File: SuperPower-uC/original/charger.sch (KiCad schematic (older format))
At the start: 24 parts, among them J2 NTC connector, J3 DNP/JST_XH_S2B_thru, Q2 DMN3018SSD, Q3 2N7002A, Q4 DMP3028LSD, U2 LTC4162EUFD-LAD

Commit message: Assigned footprint to resistors 0603 and connectors
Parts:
- C2, C3: footprint Capacitor_SMD:C_0805_2012Metric -> Capacitors_SMD:C_0805
- C4, C5: footprint Capacitor_SMD:C_0603_1608Metric -> Capacitors_SMD:C_0603
- C6, C7: footprint Capacitor_SMD:C_1206_3216Metric -> Capacitors_SMD:C_1206
- R10, R12, R13, R14, R6, R8, R9: footprint (none) -> Resistors_SMD:R_0603
- R11, R7: footprint (none) -> Resistors_SMD:R_0805
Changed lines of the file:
@@
 F 0 "R7" V 4495 2800 50  0000 C CNN
 F 1 "68m" V 4586 2800 50  0000 C CNN
-F 2 "" V 4740 2790 50  0001 C CNN
+F 2 "Resistors_SMD:R_0805" V 4740 2790 50  0001 C CNN
 F 3 "~" H 4700 2800 50  0001 C CNN
 	1    4700 2800
@@
 F 0 "R11" H 7518 4196 50  0000 L CNN
 F 1 "68m" H 7518 4105 50  0000 L CNN
-F 2 "" V 7490 4140 50  0001 C CNN
+F 2 "Resistors_SMD:R_0805" V 7490 4140 50  0001 C CNN
 F 3 "~" H 7450 4150 50  0001 C CNN
 	1    7450 4150
@@
 F 0 "R9" V 6195 4700 50  0000 C CNN
 F 1 "10k" V 6286 4700 50  0000 C CNN
-F 2 "" V 6440 4690 50  0001 C CNN
+F 2 "Resistors_SMD:R_0603" V 6440 4690 50  0001 C CNN
 F 3 "~" H 6400 4700 50  0001 C CNN
 	1    6400 4700
@@
 F 0 "R13" H 7118 2096 50  0000 L CNN
 F 1 "390k" H 7118 2005 50  0000 L CNN
-F 2 "" V 7090 2040 50  0001 C CNN
+F 2 "Resistors_SMD:R_0603" V 7090 2040 50  0001 C CNN
 F 3 "~" H 7050 2050 50  0001 C CNN
 	1    7050 2050
@@
 F 0 "R10" H 6668 1696 50  0000 L CNN
 F 1 "1M" H 6668 1605 50  0000 L CNN
-F 2 "" V 6640 1640 50  0001 C CNN
+F 2 "Resistors_SMD:R_0603" V 6640 1640 50  0001 C CNN
 F 3 "~" H 6600 1650 50  0001 C CNN
 	1    6600 1650
@@
 F 0 "R12" V 6845 850 50  0000 C CNN
 F 1 "DNP/0" V 6936 850 50  0000 C CNN
-F 2 "" V 7090 840 50  0001 C CNN
+F 2 "Resistors_SMD:R_0603" V 7090 840 50  0001 C CNN
 F 3 "~" H 7050 850 50  0001 C CNN
 	1    7050 850
@@
 F 0 "R6" V 2345 3750 50  0000 C CNN
 F 1 "2.2k" V 2436 3750 50  0000 C CNN
-F 2 "" V 2590 3740 50  0001 C CNN
+F 2 "Resistors_SMD:R_0603" V 2590 3740 50  0001 C CNN
 F 3 "~" H 2550 3750 50  0001 C CNN
 	1    2550 3750
@@
 F 0 "R8" H 5232 5304 50  0000 R CNN
 F 1 "63.4k" H 5232 5395 50  0000 R CNN
-F 2 "" V 5340 5340 50  0001 C CNN
+F 2 "Resistors_SMD:R_0603" V 5340 5340 50  0001 C CNN
 F 3 "~" H 5300 5350 50  0001 C CNN
 	1    5300 5350
@@
 F 0 "R14" V 6195 5100 50  0000 C CNN
 F 1 "10k" V 6286 5100 50  0000 C CNN
-F 2 "" V 6440 5090 50  0001 C CNN
+F 2 "Resistors_SMD:R_0603" V 6440 5090 50  0001 C CNN
 F 3 "~" H 6400 5100 50  0001 C CNN
 	1    6400 5100
@@
 F 0 "C7" H 8415 3532 50  0000 L CNN
 F 1 "CL31B106KAHNNNE" H 8325 3250 50  0001 L CNN
-F 2 "Capacitor_SMD:C_1206_3216Metric" H 8338 3200 50  0001 C CNN
+F 2 "Capacitors_SMD:C_1206" H 8338 3200 50  0001 C CNN
 F 3 "https://eu.mouser.com/datasheet/2/585/MLCC-1837944.pdf" H 8300 3350 50  0001 C CNN
 F 4 "Samsung" H 8300 3350 50  0001 C CNN "Mfr_name"
@@
 F 0 "C6" H 7565 4782 50  0000 L CNN
 F 1 "CL31B106KAHNNNE" H 7475 4500 50  0001 L CNN
-F 2 "Capacitor_SMD:C_1206_3216Metric" H 7488 4450 50  0001 C CNN
+F 2 "Capacitors_SMD:C_1206" H 7488 4450 50  0001 C CNN
 F 3 "https://eu.mouser.com/datasheet/2/585/MLCC-1837944.pdf" H 7450 4600 50  0001 C CNN
 F 4 "Samsung" H 7450 4600 50  0001 C CNN "Mfr_name"
@@
 F 0 "C2" H 3465 3232 50  0000 L CNN
 F 1 "CC0603JRX7R9BB104" H 3375 2950 50  0001 L CNN
-F 2 "Capacitor_SMD:C_0805_2012Metric" H 3388 2900 50  0001 C CNN
+F 2 "Capacitors_SMD:C_0805" H 3388 2900 50  0001 C CNN
 F 3 "https://www.yageo.com/upload/media/product/productsearch/datasheet/mlcc/UPY-GPHC_X7R_6.3V-to-50V_20.pdf" H 3350 3050 50  0001 C CNN
 F 4 "Yageo" H 3350 3050 50  0001 C CNN "Mfr_name"
@@
 F 0 "C4" H 4865 5082 50  0000 L CNN
 F 1 "CL10B105KO8NNNC" H 4775 4800 50  0001 L CNN
-F 2 "Capacitor_SMD:C_0603_1608Metric" H 4788 4750 50  0001 C CNN
+F 2 "Capacitors_SMD:C_0603" H 4788 4750 50  0001 C CNN
 F 3 "" H 4750 4900 50  0001 C CNN
 F 4 "Samsung" H 4750 4900 50  0001 C CNN "Mfr_name"
@@
 F 0 "C3" H 4365 5082 50  0000 L CNN
 F 1 "TMK212AB7475KG-T" H 4275 4800 50  0001 L CNN
-F 2 "Capacitor_SMD:C_0805_2012Metric" H 4288 4750 50  0001 C CNN
+F 2 "Capacitors_SMD:C_0805" H 4288 4750 50  0001 C CNN
 F 3 "https://eu.mouser.com/datasheet/2/396/mlcc02_e-1307760.pdf" H 4250 4900 50  0001 C CNN
 F 4 "Taiyo Yuden" H 4250 4900 50  0001 C CNN "Mfr_name"
@@
 F 0 "C5" H 6515 3832 50  0000 L CNN
 F 1 "CL10B223KB8NNNC" H 6425 3550 50  0001 L CNN
-F 2 "Capacitor_SMD:C_0603_1608Metric" H 6438 3500 50  0001 C CNN
+F 2 "Capacitors_SMD:C_0603" H 6438 3500 50  0001 C CNN
 F 3 "" H 6400 3650 50  0001 C CNN
 F 4 "CL10B223KB8NNNC" H 6400 3650 50  0001 C CNN "Mfr_no"

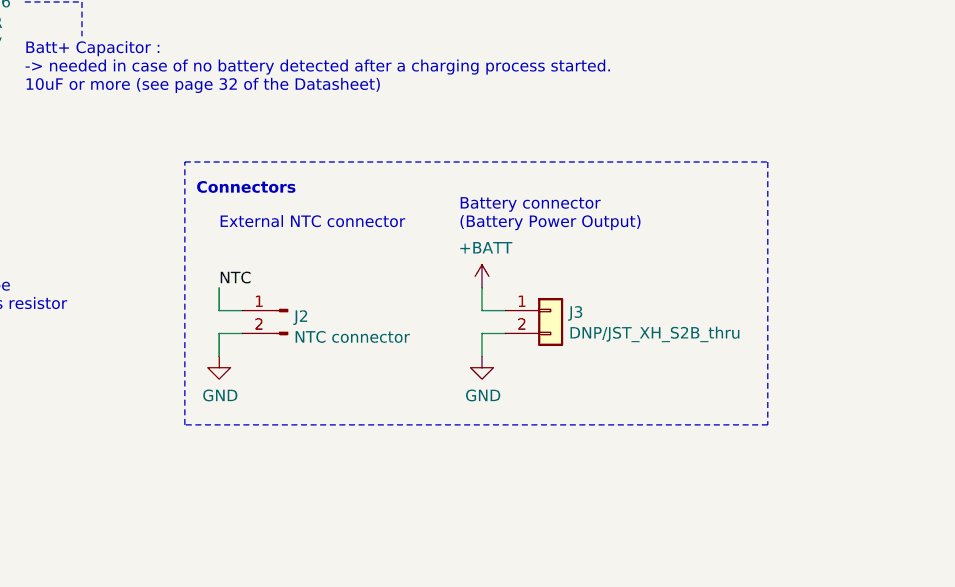
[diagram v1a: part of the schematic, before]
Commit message: Update NTC Connector & USB-C Library path
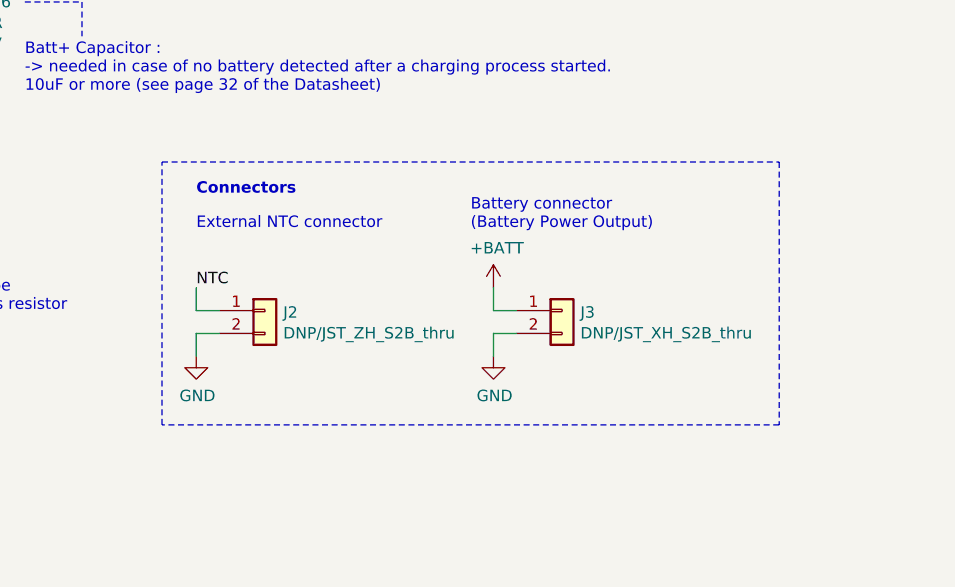
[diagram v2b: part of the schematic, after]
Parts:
- removed J2: NTC connector, symbol Connector:Conn_01x02_Male
- added J2: DNP/JST_ZH_S2B_thru, Connector_JST_user:JST_ZH_S2B-ZR_1x02_P1.50mm_Horizontal, symbol jst_zh_s2b_thru:JST_ZH_S2B_thru
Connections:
- net GND: now also J2.2 (Pin_2)
- net NTC: now also J2.1 (Pin_1)
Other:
- moved on the sheet: J3

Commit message: Updated footprints and fixed issues
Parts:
- J2: footprint Connector_JST_user:JST_ZH_S2B-ZR_1x02_P1.50mm_Horizontal -> JST_ZH_S2B_THRU:JST_ZH_S2B-ZR_1x02_P1.50mm_Horizontal
- J3: footprint Connector_JST:JST_XH_S2B-XH-A_1x02_P2.50mm_Horizontal -> Connectors_JST:JST_XH_S02B-XH-A_02x2.50mm_Angled
- LED1: footprint (none) -> LEDs:LED_0603
- Q3: footprint Package_TO_SOT_SMD:SOT-23 -> TO_SOT_Packages_SMD:SOT-23
- U2: footprint Package_DFN_QFN:QFN-28-1EP_4x5mm_P0.5mm_EP2.65x3.65mm_ThermalVias -> Housings_DFN_QFN:QFN-28-1EP_4x5mm_Pitch0.5mm
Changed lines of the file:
@@
 F 0 "U2" H 5200 5050 50  0000 C CNN
 F 1 "LTC4162EUFD-LAD" H 5950 5050 50  0000 C CNN
-F 2 "Package_DFN_QFN:QFN-28-1EP_4x5mm_P0.5mm_EP2.65x3.65mm_ThermalVias" H 5250 5050 50  0001 C CNN
+F 2 "Housings_DFN_QFN:QFN-28-1EP_4x5mm_Pitch0.5mm" H 5250 5050 50  0001 C CNN
 F 3 "https://www.analog.com/media/en/technical-documentation/data-sheets/LTC4162-L.pdf" H 5200 5050 50  0001 C CNN
 F 4 "https://octopart.com/ltc4162eufd-lad%23pbf-analog+devices-92333982?r=sp" H 5600 4000 50  0001 C CNN "Octopart_link"
@@
 F 0 "LED1" H 2143 3495 50  0000 C CNN
 F 1 "150060YS75000_0603" H 2143 3586 50  0001 C CNN
-F 2 "" H 2150 3750 50  0001 C CNN
+F 2 "LEDs:LED_0603" H 2150 3750 50  0001 C CNN
 F 3 "~" H 2150 3750 50  0001 C CNN
 F 4 "Wurth Elektronik " H 2150 3750 50  0001 C CNN "Mfr_name"
@@
 F 0 "J3" H 10230 5942 50  0000 L CNN
 F 1 "DNP/JST_XH_S2B_thru" H 10230 5851 50  0000 L CNN
-F 2 "Connector_JST:JST_XH_S2B-XH-A_1x02_P2.50mm_Horizontal" H 10150 5950 50  0001 C CNN
+F 2 "Connectors_JST:JST_XH_S02B-XH-A_02x2.50mm_Angled" H 10150 5950 50  0001 C CNN
 F 3 "http://www.jst-mfg.com/product/pdf/eng/eXH.pdf" H 10150 5950 50  0001 C CNN
 F 4 "JST" H 10150 5950 50  0001 C CNN "Mfr_name"
@@
 F 0 "Q3" H 7155 2587 50  0000 L CNN
 F 1 "2N7002A" H 7155 2496 50  0000 L CNN
-F 2 "Package_TO_SOT_SMD:SOT-23" H 7150 2375 50  0001 L CNN
+F 2 "TO_SOT_Packages_SMD:SOT-23" H 7150 2375 50  0001 L CNN
 F 3 "https://www.diodes.com/assets/Datasheets/ds31360.pdf" H 6950 2450 50  0001 C CNN
 F 4 "Diodes Incorporated" H 6950 2450 50  0001 C CNN "Mfr_name"
@@
 F 0 "J2" H 8930 5942 50  0000 L CNN
 F 1 "DNP/JST_ZH_S2B_thru" H 8930 5851 50  0000 L CNN
-F 2 "Connector_JST_user:JST_ZH_S2B-ZR_1x02_P1.50mm_Horizontal" H 8850 5950 50  0001 C CNN
+F 2 "JST_ZH_S2B_THRU:JST_ZH_S2B-ZR_1x02_P1.50mm_Horizontal" H 8850 5950 50  0001 C CNN
 F 3 "http://www.jst-mfg.com/product/pdf/eng/eZH.pdf" H 8850 5950 50  0001 C CNN
 F 4 "JST" H 8850 5950 50  0001 C CNN "Mfr_name"

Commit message: reassigned most footprints
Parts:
- C2, C3: footprint Capacitors_SMD:C_0805 -> Capacitor_SMD:C_0805_2012Metric
- C4, C5: footprint Capacitors_SMD:C_0603 -> Capacitor_SMD:C_0603_1608Metric
- C6, C7: footprint Capacitors_SMD:C_1206 -> Capacitor_SMD:C_1206_3216Metric
- J3: footprint Connectors_JST:JST_XH_S02B-XH-A_02x2.50mm_Angled -> Connector_JST:JST_XH_S2B-XH-A-1_1x02_P2.50mm_Horizontal
- LED1: footprint LEDs:LED_0603 -> LED_SMD:LED_0603_1608Metric
- Q3: footprint TO_SOT_Packages_SMD:SOT-23 -> Package_TO_SOT_SMD:SOT-23
- R10, R12, R13, R14, R6, R8, R9: footprint Resistors_SMD:R_0603 -> Resistor_SMD:R_0603_1608Metric
- R11, R7: footprint Resistors_SMD:R_0805 -> Resistor_SMD:R_0805_2012Metric
- U2: footprint Housings_DFN_QFN:QFN-28-1EP_4x5mm_Pitch0.5mm -> Package_DFN_QFN:QFN-28-1EP_4x5mm_P0.5mm_EP2.65x3.65mm_ThermalVias
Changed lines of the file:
@@
 F 0 "R7" V 4495 2800 50  0000 C CNN
 F 1 "68m" V 4586 2800 50  0000 C CNN
-F 2 "Resistors_SMD:R_0805" V 4740 2790 50  0001 C CNN
+F 2 "Resistor_SMD:R_0805_2012Metric" V 4740 2790 50  0001 C CNN
 F 3 "~" H 4700 2800 50  0001 C CNN
 	1    4700 2800
@@
 F 0 "R11" H 7518 4196 50  0000 L CNN
 F 1 "68m" H 7518 4105 50  0000 L CNN
-F 2 "Resistors_SMD:R_0805" V 7490 4140 50  0001 C CNN
+F 2 "Resistor_SMD:R_0805_2012Metric" V 7490 4140 50  0001 C CNN
 F 3 "~" H 7450 4150 50  0001 C CNN
 	1    7450 4150
@@
 F 0 "R9" V 6195 4700 50  0000 C CNN
 F 1 "10k" V 6286 4700 50  0000 C CNN
-F 2 "Resistors_SMD:R_0603" V 6440 4690 50  0001 C CNN
+F 2 "Resistor_SMD:R_0603_1608Metric" V 6440 4690 50  0001 C CNN
 F 3 "~" H 6400 4700 50  0001 C CNN
 	1    6400 4700
@@
 F 0 "R13" H 7118 2096 50  0000 L CNN
 F 1 "390k" H 7118 2005 50  0000 L CNN
-F 2 "Resistors_SMD:R_0603" V 7090 2040 50  0001 C CNN
+F 2 "Resistor_SMD:R_0603_1608Metric" V 7090 2040 50  0001 C CNN
 F 3 "~" H 7050 2050 50  0001 C CNN
 	1    7050 2050
@@
 F 0 "R10" H 6668 1696 50  0000 L CNN
 F 1 "1M" H 6668 1605 50  0000 L CNN
-F 2 "Resistors_SMD:R_0603" V 6640 1640 50  0001 C CNN
+F 2 "Resistor_SMD:R_0603_1608Metric" V 6640 1640 50  0001 C CNN
 F 3 "~" H 6600 1650 50  0001 C CNN
 	1    6600 1650
@@
 F 0 "R12" V 6845 850 50  0000 C CNN
 F 1 "DNP/0" V 6936 850 50  0000 C CNN
-F 2 "Resistors_SMD:R_0603" V 7090 840 50  0001 C CNN
+F 2 "Resistor_SMD:R_0603_1608Metric" V 7090 840 50  0001 C CNN
 F 3 "~" H 7050 850 50  0001 C CNN
 	1    7050 850
@@
 F 0 "R6" V 2345 3750 50  0000 C CNN
 F 1 "2.2k" V 2436 3750 50  0000 C CNN
-F 2 "Resistors_SMD:R_0603" V 2590 3740 50  0001 C CNN
+F 2 "Resistor_SMD:R_0603_1608Metric" V 2590 3740 50  0001 C CNN
 F 3 "~" H 2550 3750 50  0001 C CNN
 	1    2550 3750
@@
 F 0 "R8" H 5232 5304 50  0000 R CNN
 F 1 "63.4k" H 5232 5395 50  0000 R CNN
-F 2 "Resistors_SMD:R_0603" V 5340 5340 50  0001 C CNN
+F 2 "Resistor_SMD:R_0603_1608Metric" V 5340 5340 50  0001 C CNN
 F 3 "~" H 5300 5350 50  0001 C CNN
 	1    5300 5350
@@
 F 0 "U2" H 5200 5050 50  0000 C CNN
 F 1 "LTC4162EUFD-LAD" H 5950 5050 50  0000 C CNN
-F 2 "Housings_DFN_QFN:QFN-28-1EP_4x5mm_Pitch0.5mm" H 5250 5050 50  0001 C CNN
+F 2 "Package_DFN_QFN:QFN-28-1EP_4x5mm_P0.5mm_EP2.65x3.65mm_ThermalVias" H 5250 5050 50  0001 C CNN
 F 3 "https://www.analog.com/media/en/technical-documentation/data-sheets/LTC4162-L.pdf" H 5200 5050 50  0001 C CNN
 F 4 "https://octopart.com/ltc4162eufd-lad%23pbf-analog+devices-92333982?r=sp" H 5600 4000 50  0001 C CNN "Octopart_link"
@@
 F 0 "LED1" H 2143 3495 50  0000 C CNN
 F 1 "150060YS75000_0603" H 2143 3586 50  0001 C CNN
-F 2 "LEDs:LED_0603" H 2150 3750 50  0001 C CNN
+F 2 "LED_SMD:LED_0603_1608Metric" H 2150 3750 50  0001 C CNN
 F 3 "~" H 2150 3750 50  0001 C CNN
 F 4 "Wurth Elektronik " H 2150 3750 50  0001 C CNN "Mfr_name"
@@
 F 0 "R14" V 6195 5100 50  0000 C CNN
 F 1 "10k" V 6286 5100 50  0000 C CNN
-F 2 "Resistors_SMD:R_0603" V 6440 5090 50  0001 C CNN
+F 2 "Resistor_SMD:R_0603_1608Metric" V 6440 5090 50  0001 C CNN
 F 3 "~" H 6400 5100 50  0001 C CNN
 	1    6400 5100
@@
 F 0 "C7" H 8415 3532 50  0000 L CNN
 F 1 "CL31B106KAHNNNE" H 8325 3250 50  0001 L CNN
-F 2 "Capacitors_SMD:C_1206" H 8338 3200 50  0001 C CNN
+F 2 "Capacitor_SMD:C_1206_3216Metric" H 8338 3200 50  0001 C CNN
 F 3 "https://eu.mouser.com/datasheet/2/585/MLCC-1837944.pdf" H 8300 3350 50  0001 C CNN
 F 4 "Samsung" H 8300 3350 50  0001 C CNN "Mfr_name"
@@
 F 0 "C6" H 7565 4782 50  0000 L CNN
 F 1 "CL31B106KAHNNNE" H 7475 4500 50  0001 L CNN
-F 2 "Capacitors_SMD:C_1206" H 7488 4450 50  0001 C CNN
+F 2 "Capacitor_SMD:C_1206_3216Metric" H 7488 4450 50  0001 C CNN
 F 3 "https://eu.mouser.com/datasheet/2/585/MLCC-1837944.pdf" H 7450 4600 50  0001 C CNN
 F 4 "Samsung" H 7450 4600 50  0001 C CNN "Mfr_name"
@@
 F 0 "C2" H 3465 3232 50  0000 L CNN
 F 1 "CC0603JRX7R9BB104" H 3375 2950 50  0001 L CNN
-F 2 "Capacitors_SMD:C_0805" H 3388 2900 50  0001 C CNN
+F 2 "Capacitor_SMD:C_0805_2012Metric" H 3388 2900 50  0001 C CNN
 F 3 "https://www.yageo.com/upload/media/product/productsearch/datasheet/mlcc/UPY-GPHC_X7R_6.3V-to-50V_20.pdf" H 3350 3050 50  0001 C CNN
 F 4 "Yageo" H 3350 3050 50  0001 C CNN "Mfr_name"
@@
 F 0 "C4" H 4865 5082 50  0000 L CNN
 F 1 "CL10B105KO8NNNC" H 4775 4800 50  0001 L CNN
-F 2 "Capacitors_SMD:C_0603" H 4788 4750 50  0001 C CNN
+F 2 "Capacitor_SMD:C_0603_1608Metric" H 4788 4750 50  0001 C CNN
 F 3 "" H 4750 4900 50  0001 C CNN
 F 4 "Samsung" H 4750 4900 50  0001 C CNN "Mfr_name"
@@
 F 0 "C3" H 4365 5082 50  0000 L CNN
 F 1 "TMK212AB7475KG-T" H 4275 4800 50  0001 L CNN
-F 2 "Capacitors_SMD:C_0805" H 4288 4750 50  0001 C CNN
+F 2 "Capacitor_SMD:C_0805_2012Metric" H 4288 4750 50  0001 C CNN
 F 3 "https://eu.mouser.com/datasheet/2/396/mlcc02_e-1307760.pdf" H 4250 4900 50  0001 C CNN
 F 4 "Taiyo Yuden" H 4250 4900 50  0001 C CNN "Mfr_name"
@@
 F 0 "C5" H 6515 3832 50  0000 L CNN
 F 1 "CL10B223KB8NNNC" H 6425 3550 50  0001 L CNN
-F 2 "Capacitors_SMD:C_0603" H 6438 3500 50  0001 C CNN
+F 2 "Capacitor_SMD:C_0603_1608Metric" H 6438 3500 50  0001 C CNN
 F 3 "" H 6400 3650 50  0001 C CNN
 F 4 "CL10B223KB8NNNC" H 6400 3650 50  0001 C CNN "Mfr_no"
@@
 F 0 "J3" H 10230 5942 50  0000 L CNN
 F 1 "DNP/JST_XH_S2B_thru" H 10230 5851 50  0000 L CNN
-F 2 "Connectors_JST:JST_XH_S02B-XH-A_02x2.50mm_Angled" H 10150 5950 50  0001 C CNN
+F 2 "Connector_JST:JST_XH_S2B-XH-A-1_1x02_P2.50mm_Horizontal" H 10150 5950 50  0001 C CNN
 F 3 "http://www.jst-mfg.com/product/pdf/eng/eXH.pdf" H 10150 5950 50  0001 C CNN
 F 4 "JST" H 10150 5950 50  0001 C CNN "Mfr_name"
@@
 F 0 "Q3" H 7155 2587 50  0000 L CNN
 F 1 "2N7002A" H 7155 2496 50  0000 L CNN
-F 2 "TO_SOT_Packages_SMD:SOT-23" H 7150 2375 50  0001 L CNN
+F 2 "Package_TO_SOT_SMD:SOT-23" H 7150 2375 50  0001 L CNN
 F 3 "https://www.diodes.com/assets/Datasheets/ds31360.pdf" H 6950 2450 50  0001 C CNN
 F 4 "Diodes Incorporated" H 6950 2450 50  0001 C CNN "Mfr_name"
